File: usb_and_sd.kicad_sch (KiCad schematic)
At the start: 72 parts, among them J7001 USB_C_Receptacle_USB2.0_16P, J7002 USB_A, J7003 Micro_SD_Card_Det1, U1001 AM6231ASGGGAALW, U7001 TVS0500DRVR, U7002 KLMAG2GEUF-B04P, U7004 TPD3S014, U7005 TPS22918DBVR

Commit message: Finished USB A routing. Started micro sd routing
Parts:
- C7016: footprint Capacitor_SMD:C_0201_0603Metric -> Capacitor_SMD:C_0402_1005Metric
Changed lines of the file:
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@@
 	)
 	(junction
+		(at 203.2 191.77)
+		(diameter 0)
+		(color 0 0 0 0)
+	)
+	(junction
 		(at 238.76 205.74)
 		(diameter 0)
@@
 	)
 	(junction
+		(at 207.01 196.85)
+		(diameter 0)
+		(color 0 0 0 0)
+	)
+	(junction
 		(at 656.59 121.92)
 		(diameter 0)
@@
 	)
 	(junction
-		(at 203.2 191.77)
-		(diameter 0)
-		(color 0 0 0 0)
-	)
-	(junction
 		(at 171.45 266.7)
 		(diameter 0)
@@
 	)
 	(junction
-		(at 207.01 196.85)
-		(diameter 0)
-		(color 0 0 0 0)
-	)
-	(junction
 		(at 585.47 325.12)
 		(diameter 0)
@@
 	(wire
 		(pts
-			(xy 219.71 191.77) (xy 203.2 191.77)
-		)
-		(stroke
-			(width 0)
-			(type default)
-		)
-	)
-	(wire
-		(pts
 			(xy 615.95 374.65) (xy 615.95 382.27)
 		)
@@
 	(wire
 		(pts
-			(xy 537.21 383.54) (xy 544.83 383.54)
+			(xy 207.01 196.85) (xy 217.17 196.85)
 		)
 		(stroke
@@
 	(wire
 		(pts
-			(xy 391.16 156.21) (xy 407.67 156.21)
-		)
-		(stroke
-			(width 0)
-			(type default)
-		)
-	)
-	(wire
-		(pts
-			(xy 571.5 201.93) (xy 571.5 203.2)
+			(xy 537.21 383.54) (xy 544.83 383.54)
 		)
 		(stroke
@@
 	(wire
 		(pts
-			(xy 207.01 251.46) (xy 207.01 196.85)
+			(xy 391.16 156.21) (xy 407.67 156.21)
 		)
 		(stroke
@@
 	(wire
 		(pts
-			(xy 203.2 248.92) (xy 203.2 191.77)
+			(xy 571.5 201.93) (xy 571.5 203.2)
 		)
 		(stroke
@@
 	(wire
 		(pts
+			(xy 203.2 191.77) (xy 219.71 191.77)
+		)
+		(stroke
+			(width 0)
+			(type default)
+		)
+	)
+	(wire
+		(pts
 			(xy 609.6 137.16) (xy 612.14 137.16)
 		)
@@
 	(wire
 		(pts
+			(xy 207.01 196.85) (xy 207.01 251.46)
+		)
+		(stroke
+			(width 0)
+			(type default)
+		)
+	)
+	(wire
+		(pts
 			(xy 104.14 212.09) (xy 111.76 212.09)
 		)
@@
 	(wire
 		(pts
-			(xy 172.72 191.77) (xy 203.2 191.77)
-		)
-		(stroke
-			(width 0)
-			(type default)
-		)
-	)
-	(wire
-		(pts
 			(xy 576.58 374.65) (xy 576.58 383.54)
 		)
@@
 	(wire
 		(pts
-			(xy 217.17 196.85) (xy 207.01 196.85)
-		)
-		(stroke
-			(width 0)
-			(type default)
-		)
-	)
-	(wire
-		(pts
 			(xy 560.07 378.46) (xy 560.07 383.54)
 		)
@@
 	(wire
 		(pts
+			(xy 203.2 191.77) (xy 203.2 248.92)
+		)
+		(stroke
+			(width 0)
+			(type default)
+		)
+	)
+	(wire
+		(pts
 			(xy 190.5 128.27) (xy 190.5 130.81)
 		)
@@
 	(wire
 		(pts
+			(xy 172.72 191.77) (xy 203.2 191.77)
+		)
+		(stroke
+			(width 0)
+			(type default)
+		)
+	)
+	(wire
+		(pts
 			(xy 492.76 294.64) (xy 520.7 294.64)
 		)
@@
 			)
 		)
-		(property "Footprint" "Capacitor_SMD:C_0201_0603Metric"
+		(property "Footprint" "Capacitor_SMD:C_0402_1005Metric"
 			(at 172.4152 264.16 0)
 			(effects

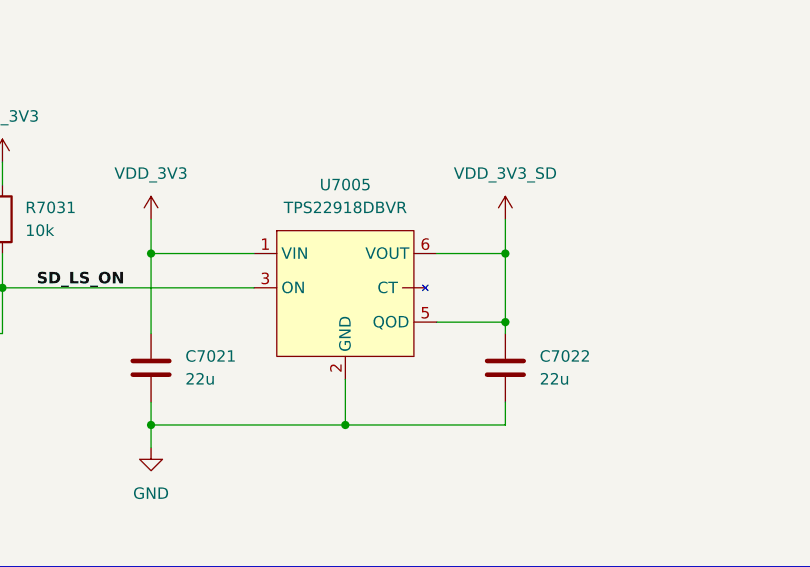
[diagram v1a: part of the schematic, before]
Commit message: More micro SD routing
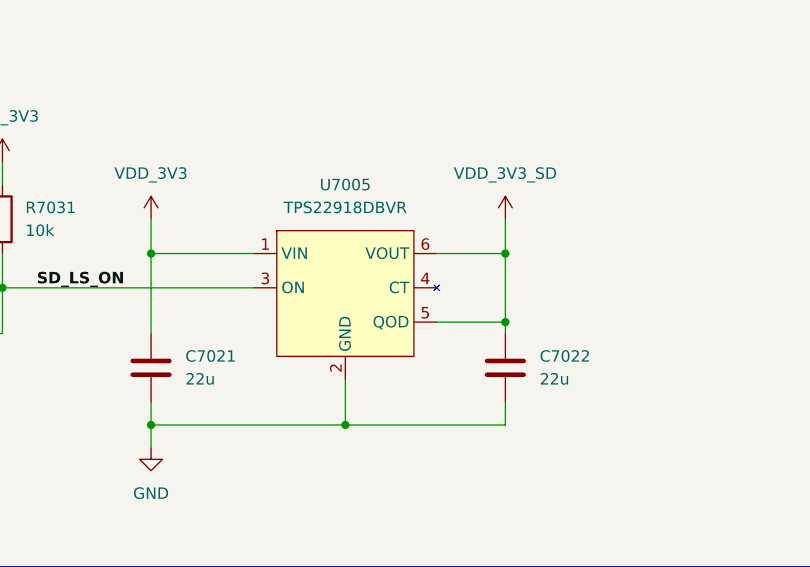
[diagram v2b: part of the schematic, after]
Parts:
- C7019, C7020: footprint Capacitor_SMD:C_0201_0603Metric -> Capacitor_SMD:C_0402_1005Metric
- D7001, D7002: footprint Diode_SMD:D_0402_1005Metric -> SoftServicesFootprintLibrary:TPD1E1B04DPYR
- D7006, D7007, D7008, D7009, D7010, D7011, D7012: footprint Diode_SMD:D_SOD-882 -> SoftServicesFootprintLibrary:TPD1E1B04DPYR
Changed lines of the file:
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@@
 			)
 		)
-		(property "Footprint" "Capacitor_SMD:C_0201_0603Metric"
+		(property "Footprint" "Capacitor_SMD:C_0402_1005Metric"
 			(at 586.4352 322.58 0)
 			(effects
@@
 			)
 		)
-		(property "Footprint" "Diode_SMD:D_0402_1005Metric"
+		(property "Footprint" "SoftServicesFootprintLibrary:TPD1E1B04DPYR"
 			(at 184.15 161.29 0)
 			(effects
@@
 			)
 		)
-		(property "Footprint" "Diode_SMD:D_SOD-882"
+		(property "Footprint" "SoftServicesFootprintLibrary:TPD1E1B04DPYR"
 			(at 561.34 318.77 0)
 			(effects
@@
 			)
 		)
-		(property "Footprint" "Diode_SMD:D_SOD-882"
+		(property "Footprint" "SoftServicesFootprintLibrary:TPD1E1B04DPYR"
 			(at 530.86 318.77 0)
 			(effects
@@
 			)
 		)
-		(property "Footprint" "Capacitor_SMD:C_0201_0603Metric"
+		(property "Footprint" "Capacitor_SMD:C_0402_1005Metric"
 			(at 599.1352 322.58 0)
 			(effects
@@
 			)
 		)
-		(property "Footprint" "Diode_SMD:D_0402_1005Metric"
+		(property "Footprint" "SoftServicesFootprintLibrary:TPD1E1B04DPYR"
 			(at 172.72 161.29 0)
 			(effects
@@
 			)
 		)
-		(property "Footprint" "Diode_SMD:D_SOD-882"
+		(property "Footprint" "SoftServicesFootprintLibrary:TPD1E1B04DPYR"
 			(at 623.57 321.31 0)
 			(effects
@@
 			)
 		)
-		(property "Footprint" "Diode_SMD:D_SOD-882"
+		(property "Footprint" "SoftServicesFootprintLibrary:TPD1E1B04DPYR"
 			(at 551.18 318.77 0)
 			(effects
@@
 			)
 		)
-		(property "Footprint" "Diode_SMD:D_SOD-882"
+		(property "Footprint" "SoftServicesFootprintLibrary:TPD1E1B04DPYR"
 			(at 541.02 318.77 0)
 			(effects
@@
 		(pin "1"
 		)
-		(pin ""
+		(pin "4"
 		)
 		(instances
@@
 			)
 		)
-		(property "Footprint" "Diode_SMD:D_SOD-882"
+		(property "Footprint" "SoftServicesFootprintLibrary:TPD1E1B04DPYR"
 			(at 520.7 318.77 0)
 			(effects
@@
 			)
 		)
-		(property "Footprint" "Diode_SMD:D_SOD-882"
+		(property "Footprint" "SoftServicesFootprintLibrary:TPD1E1B04DPYR"
 			(at 510.54 318.77 0)
 			(effects

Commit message: Added new radio schematic
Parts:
- renumbered C7001 to C6001, C7002 to C6002, C7006 to C6003, C7010 to C6004, C7011 to C6005, C7012 to C6006, C7013 to C6007, C7014 to C6008, C7023 to C6009, C7015 to C6010, C7016 to C6011, C7017 to C6012, C7018 to C6013, C7019 to C6014, C7020 to C6015, C7021 to C6016, C7022 to C6017, D7001 to D6001, D7002 to D6002, D7003 to D6003, D7004 to D6004, D7005 to D6005, D7006 to D6006, D7007 to D6007, D7008 to D6008, D7009 to D6009, D7010 to D6010, D7011 to D6011, D7012 to D6012, D7013 to D6013, D7014 to D6014, J7001 to J6001, J7002 to J6002, J7003 to J6003, L7001 to L6001, L7002 to L6002, R7001 to R6001, R7002 to R6002, R7003 to R6003, R7004 to R6004, R7005 to R6005, R7006 to R6006, R7007 to R6007, R7008 to R6008, R7009 to R6009, R7010 to R6010, R7011 to R6011, R7012 to R6012, R7013 to R6013, R7014 to R6014, R7015 to R6015, R7016 to R6016, R7017 to R6017, R7018 to R6018, R7019 to R6019, R7020 to R6020, R7021 to R6021, R7022 to R6022, R7023 to R6023, R7024 to R6024, R7025 to R6025, R7026 to R6026, R7027 to R6027, R7028 to R6028, R7029 to R6029, R7030 to R6030, R7031 to R6031, U1001 to U1002, U7001 to U6001, U7002 to U6002, U7004 to U6003, U7005 to U6004

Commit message: Laid out and routed boot mode resistors
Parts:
- R6014: footprint Resistor_SMD:R_0201_0603Metric -> Resistor_SMD:R_0402_1005Metric
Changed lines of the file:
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@@
 			)
 		)
-		(property "Footprint" "Resistor_SMD:R_0201_0603Metric"
+		(property "Footprint" "Resistor_SMD:R_0402_1005Metric"
 			(at 415.29 151.638 90)
 			(effects

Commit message: Routed JTAG and UART header pins for SoC
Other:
- note added: "Micro SD + eMMC"
- note added: "USB A + USB C"
- note removed: "SD + eMMC"
- note removed: "USB"
- moved on the sheet: C6006, C6007, C6010, C6011, C6012, D6001, D6002, J6001, J6002, L6001, L6002, R6002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

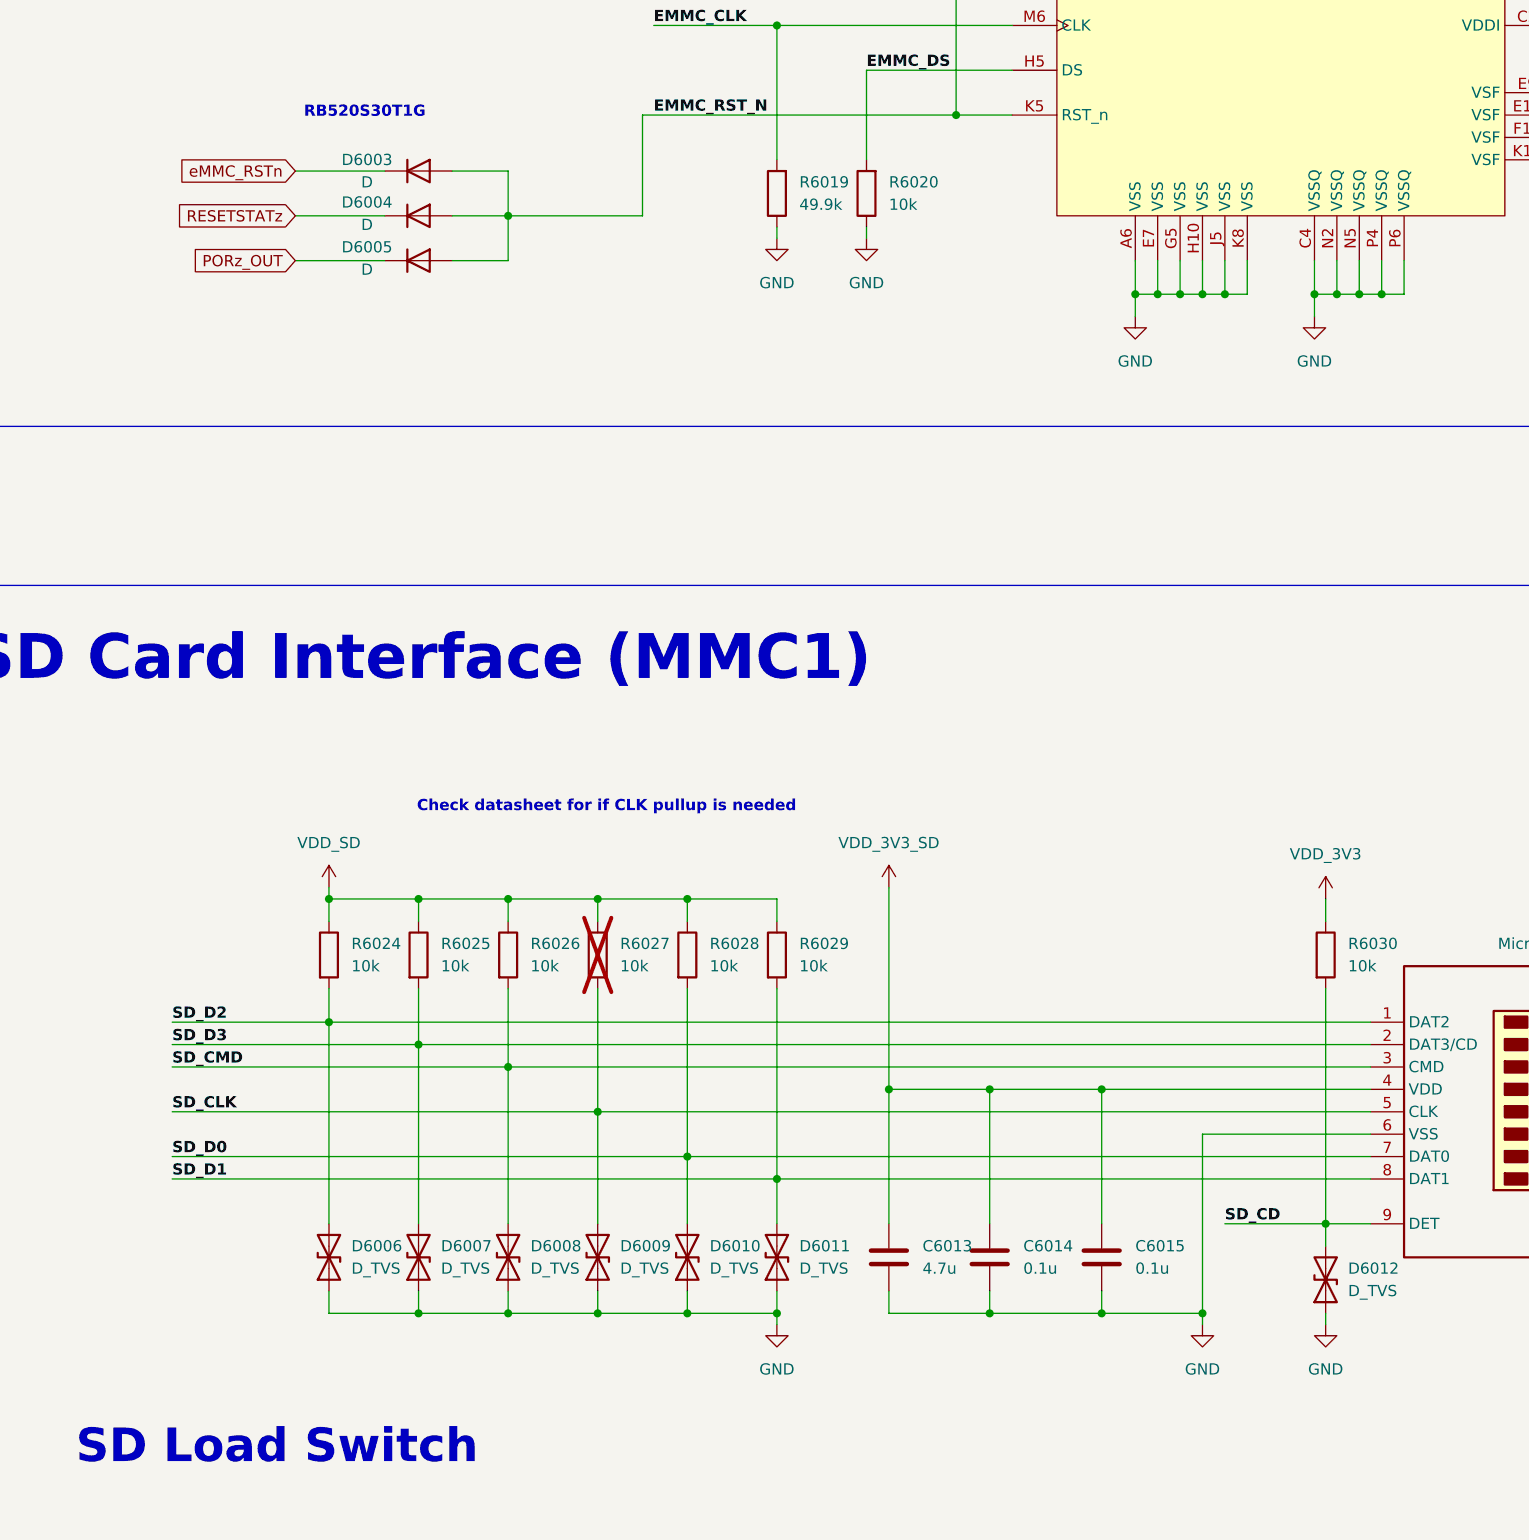
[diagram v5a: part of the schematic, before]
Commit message: Added and routed Micro SD load switch
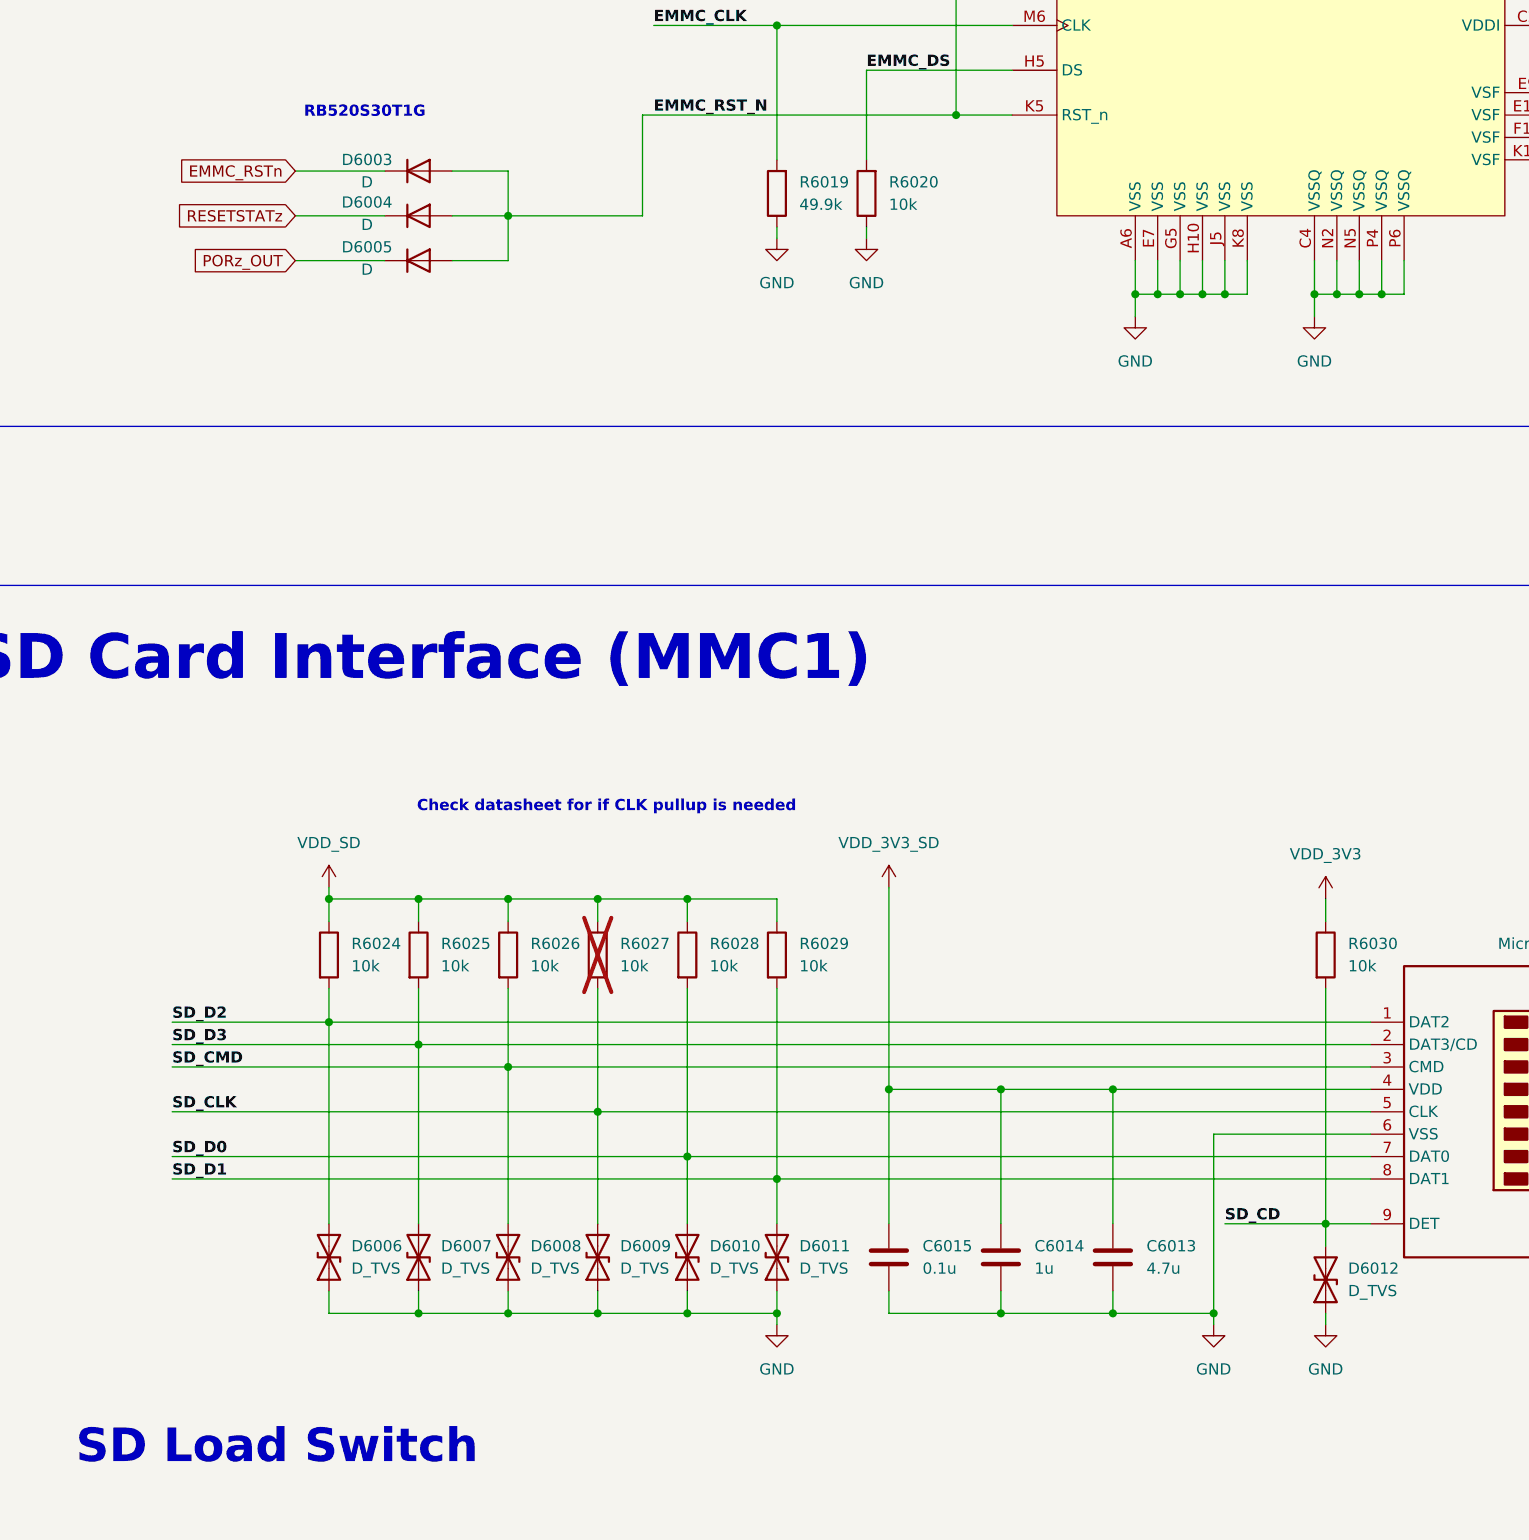
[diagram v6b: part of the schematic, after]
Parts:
- C6013: footprint Capacitor_SMD:C_0402_1005Metric -> Capacitor_SMD:C_0603_1608Metric
- C6014: value 0.1u -> 1u
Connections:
- net eMMC_RSTn renamed EMMC_RSTn
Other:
- moved on the sheet: C6013, C6014, C6015

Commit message: Small clean up
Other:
- moved on the sheet: U6002B
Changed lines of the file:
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@@
 	)
 	(rectangle
-		(start 731.52 88.9)
-		(end 820.42 271.78)
+		(start 337.82 222.25)
+		(end 426.72 405.13)
 		(stroke
 			(width 0)
@@
 	(text "Micro SD + eMMC"
 		(exclude_from_sim no)
-		(at 425.45 54.61 0)
+		(at 384.048 65.278 0)
 		(effects
 			(font
@@
 	(text "eMMC NC Pins"
 		(exclude_from_sim no)
-		(at 734.06 96.012 0)
+		(at 340.36 229.362 0)
 		(effects
 			(font
@@
 	(text "USB A + USB C"
 		(exclude_from_sim no)
-		(at 36.322 55.372 0)
+		(at 33.02 65.786 0)
 		(effects
 			(font
@@
 	(symbol
 		(lib_id "SoftServicesSymbolLibrary:KLMAG2GEUF-B04P")
-		(at 787.4 143.51 0)
+		(at 393.7 276.86 0)
 		(unit 2)
 		(exclude_from_sim no)
@@
 		(fields_autoplaced yes)
 		(property "Reference" "U6002"
-			(at 774.7 107.95 0)
+			(at 381 241.3 0)
 			(effects
 				(font
@@
 		)
 		(property "Value" "KLMAG2GEUF-B04P"
-			(at 774.7 110.49 0)
+			(at 381 243.84 0)
 			(effects
 				(font
@@
 		)
 		(property "Footprint" "Package_BGA:LFBGA-153_11.5x13mm_Layout14x14_P0.5mm"
-			(at 787.4 143.51 0)
+			(at 393.7 276.86 0)
 			(effects
 				(font
@@
 		)
 		(property "Datasheet" ""
-			(at 787.4 143.51 0)
+			(at 393.7 276.86 0)
 			(effects
 				(font
@@
 		)
 		(property "Description" ""
-			(at 787.4 143.51 0)
+			(at 393.7 276.86 0)
 			(effects
 				(font

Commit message: Fixed all warnings and almost all errors in DRC
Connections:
- net GND: now also J6002.6 (Shield), J6003.11 (SHIELD), J6003.12 (SHIELD), J6003.13 (SHIELD)
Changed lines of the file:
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@@
 	)
 	(junction
+		(at 259.08 205.74)
+		(diameter 0)
+		(color 0 0 0 0)
+	)
+	(junction
 		(at 627.38 209.55)
 		(diameter 0)
@@
 	)
 	(junction
+		(at 671.83 322.58)
+		(diameter 0)
+		(color 0 0 0 0)
+	)
+	(junction
 		(at 510.54 292.1)
 		(diameter 0)
@@
 	)
 	(junction
+		(at 671.83 317.5)
+		(diameter 0)
+		(color 0 0 0 0)
+	)
+	(junction
 		(at 541.02 156.21)
 		(diameter 0)
@@
 	)
 	(junction
+		(at 671.83 320.04)
+		(diameter 0)
+		(color 0 0 0 0)
+	)
+	(junction
 		(at 607.06 209.55)
 		(diameter 0)
@@
 	(wire
 		(pts
+			(xy 261.62 204.47) (xy 261.62 205.74)
+		)
+		(stroke
+			(width 0)
+			(type default)
+		)
+	)
+	(wire
+		(pts
 			(xy 492.76 292.1) (xy 510.54 292.1)
 		)
@@
 	(wire
 		(pts
+			(xy 671.83 320.04) (xy 671.83 322.58)
+		)
+		(stroke
+			(width 0)
+			(type default)
+		)
+	)
+	(wire
+		(pts
 			(xy 530.86 143.51) (xy 530.86 158.75)
 		)
@@
 	(wire
 		(pts
-			(xy 676.91 314.96) (xy 676.91 318.77)
+			(xy 676.91 322.58) (xy 676.91 326.39)
 		)
 		(stroke
@@
 	(wire
 		(pts
+			(xy 671.83 317.5) (xy 671.83 314.96)
+		)
+		(stroke
+			(width 0)
+			(type default)
+		)
+	)
+	(wire
+		(pts
 			(xy 220.98 191.77) (xy 237.49 191.77)
 		)
@@
 	(wire
 		(pts
+			(xy 671.83 320.04) (xy 671.83 317.5)
+		)
+		(stroke
+			(width 0)
+			(type default)
+		)
+	)
+	(wire
+		(pts
 			(xy 547.37 179.07) (xy 561.34 179.07)
 		)
@@
 	(wire
 		(pts
-			(xy 671.83 314.96) (xy 676.91 314.96)
+			(xy 671.83 322.58) (xy 676.91 322.58)
 		)
 		(stroke
@@
 	(wire
 		(pts
+			(xy 261.62 205.74) (xy 259.08 205.74)
+		)
+		(stroke
+			(width 0)
+			(type default)
+		)
+	)
+	(wire
+		(pts
 			(xy 175.26 246.38) (xy 175.26 256.54)
 		)
@@
 		(pin "1"
 		)
+		(pin "6"
+		)
 		(instances
 			(project "Leonhart"
@@
 	(symbol
 		(lib_id "power:GND")
-		(at 676.91 318.77 0)
+		(at 676.91 326.39 0)
 		(unit 1)
 		(exclude_from_sim no)
@@
 		(fields_autoplaced yes)
 		(property "Reference" "#PWR06032"
-			(at 676.91 325.12 0)
+			(at 676.91 332.74 0)
 			(effects
 				(font
@@
 		)
 		(property "Value" "GND"
-			(at 676.91 323.85 0)
+			(at 676.91 331.47 0)
 			(effects
 				(font
@@
 		)
 		(property "Footprint" ""
-			(at 676.91 318.77 0)
+			(at 676.91 326.39 0)
 			(effects
 				(font
@@
 		)
 		(property "Datasheet" ""
-			(at 676.91 318.77 0)
+			(at 676.91 326.39 0)
 			(effects
 				(font
@@
 		)
 		(property "Description" "Power symbol creates a global label with name \"GND\" , ground"
-			(at 676.91 318.77 0)
+			(at 676.91 326.39 0)
 			(effects
 				(font
@@
 		(pin "1"
 		)
+		(pin "13"
+		)
+		(pin "12"
+		)
+		(pin "11"
+		)
 		(instances
